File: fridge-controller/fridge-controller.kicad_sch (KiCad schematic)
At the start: 9 parts, among them U1 AMS1117-5.0, U2 Arduino_Pro_Mini, U3 SFH6156-2

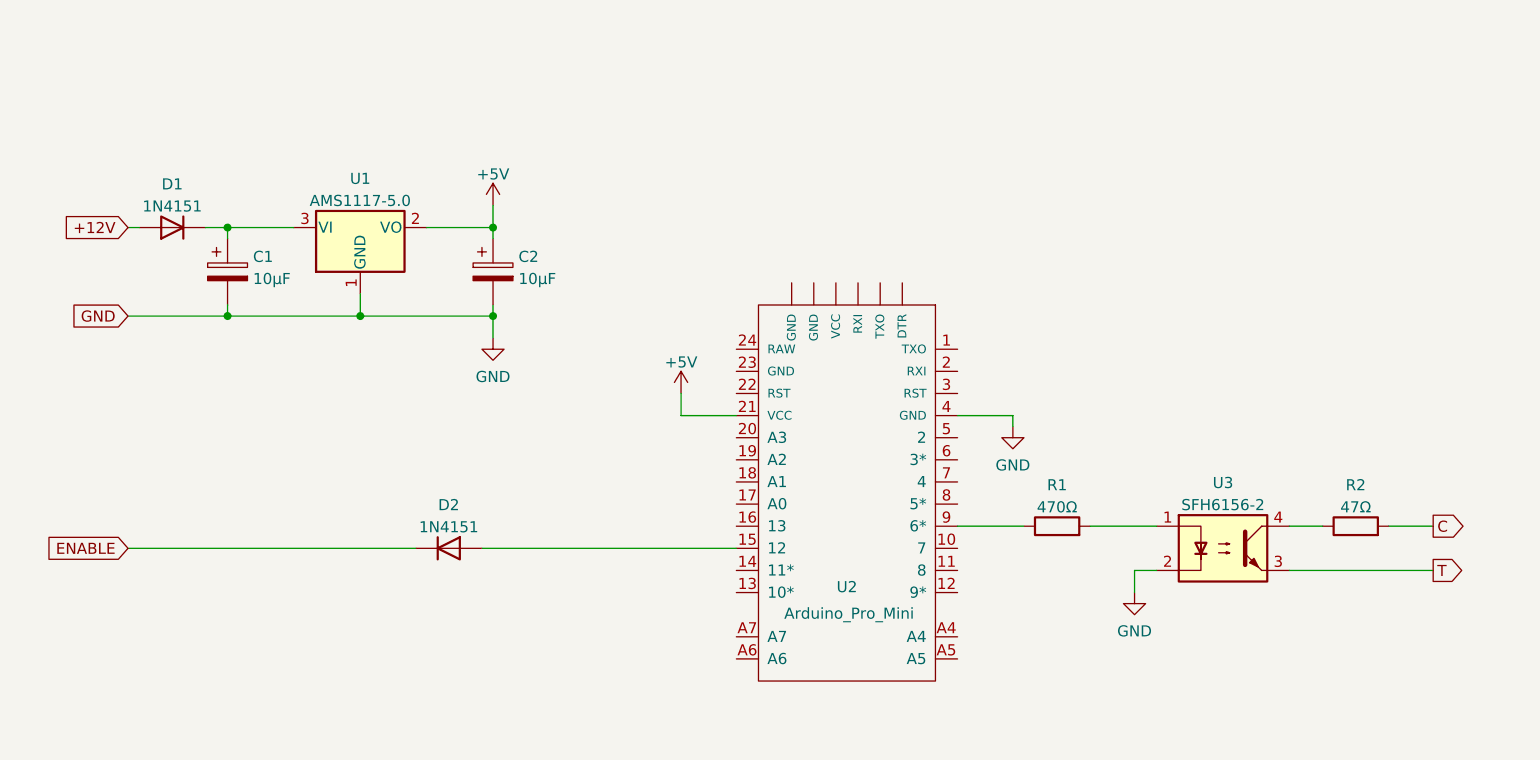
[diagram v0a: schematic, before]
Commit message: Updated fridge-controller
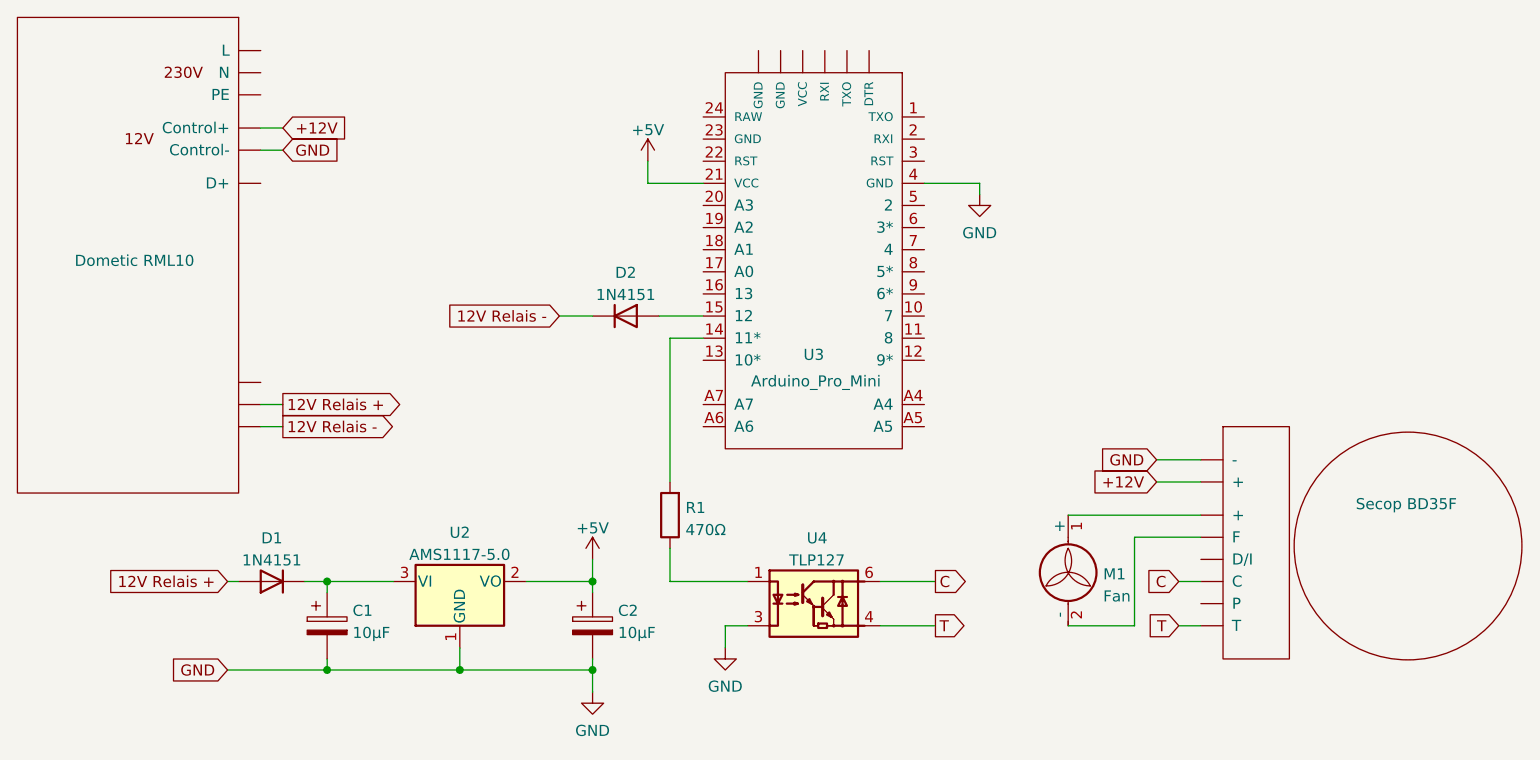
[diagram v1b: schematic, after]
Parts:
- removed R2: 47Ω, symbol Device:R
- removed U3: SFH6156-2, Package_DIP:DIP-4_W7.62mm, symbol Isolator:SFH617A-2
- added M1: Fan, symbol Motor:Fan
- added U1: Dometic RML10, symbol microfarad-de:Dometic_Fridge_2
- added U4: TLP127, Package_SO:MFSOP6-4_4.4x3.6mm_P1.27mm, symbol Isolator:TLP127
- added U5: Secop BD35F, symbol microfarad-de:Isotherm
- renumbered U1 to U2, U2 to U3
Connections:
- net +12V: now also U1. (PE), U5. (T); no longer D1.2 (A)
- net C: now also U4.6, U5. (T)
- net GND: now also U1. (PE), U4.3, U5. (T)
- net T: now also U4.4, U5. (T)
- net at R1.1: now also U4.1; no longer U3.9 (6*)
- net at R1.2: now also U3.14 (11*)
- net ENABLE renamed 12V Relais -
- net 12V Relais -: now also U1. (PE)
- new net: M1.1 (+), U5. (T)
- new net: M1.2 (-), U5. (T)
- new net 12V Relais +: D1.2 (A), U1. (PE)
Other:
- moved on the sheet: C1, C2, D1, D2, R1, U2, U3

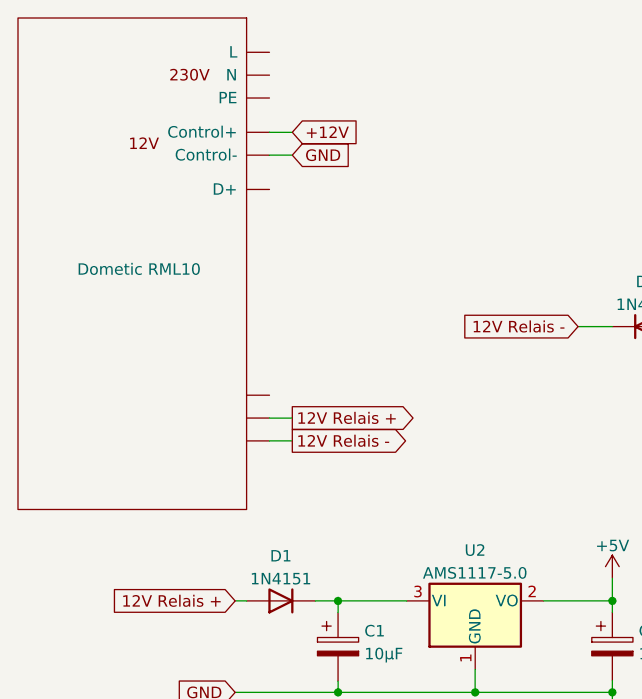
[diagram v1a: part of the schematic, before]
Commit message: Added Dometic RML10 to symbol library
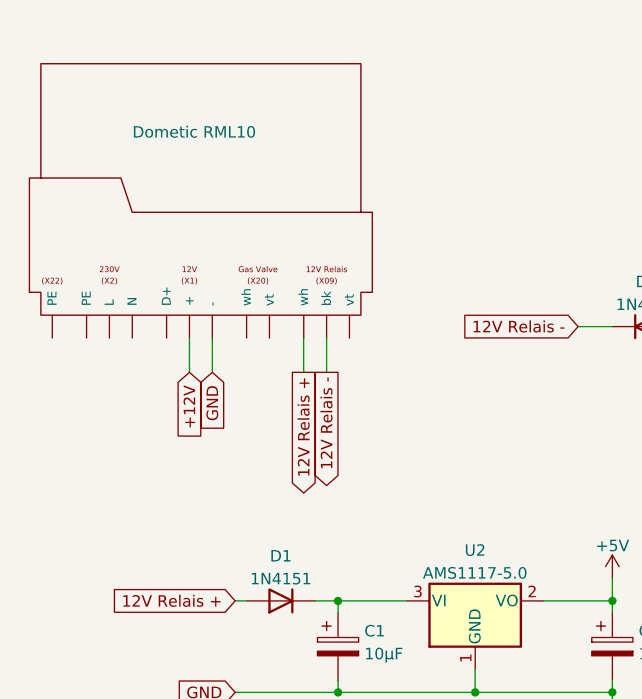
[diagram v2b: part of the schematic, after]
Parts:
- removed U1: Dometic RML10, symbol microfarad-de:Dometic_Fridge_2
- added U?: Dometic RML10, symbol microfarad-de:Dometic RML10
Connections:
- net +12V: now also U?. (wh)
- net 12V Relais +: now also U?. (wh)
- net 12V Relais -: now also U?. (wh)
- net GND: now also U?. (wh)
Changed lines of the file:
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@@
   (title_block
     (title "Secop BD35F Compressor Speed Controller")
-    (date "2025-02-09")
+    (date "2025-02-10")
     (company "Copyright (C) 2025, Karim Hraibi")
     (comment 1 "Enables variable speed control over 5 kHz PWM signal.")
@@
     (stroke (width 0) (type default) (color 0 0 0 0))
   )
-  (wire (pts (xy 46.99 27.94) (xy 49.53 27.94))
-    (stroke (width 0) (type default) (color 0 0 0 0))
-  )
   (wire (pts (xy 118.11 85.09) (xy 124.46 85.09))
     (stroke (width 0) (type default) (color 0 0 0 0))
@@
     (stroke (width 0) (type default) (color 0 0 0 0))
   )
-  (wire (pts (xy 46.99 30.48) (xy 49.53 30.48))
+  (wire (pts (xy 38.1 50.8) (xy 38.1 54.61))
     (stroke (width 0) (type default) (color 0 0 0 0))
   )
@@
     (stroke (width 0) (type default) (color 0 0 0 0))
   )
-  (wire (pts (xy 46.99 62.23) (xy 49.53 62.23))
-    (stroke (width 0) (type default) (color 0 0 0 0))
-  )
   (wire (pts (xy 139.7 72.39) (xy 154.94 72.39))
     (stroke (width 0) (type default) (color 0 0 0 0))
@@
     (stroke (width 0) (type default) (color 0 0 0 0))
   )
+  (wire (pts (xy 40.64 50.8) (xy 40.64 54.61))
+    (stroke (width 0) (type default) (color 0 0 0 0))
+  )
   (wire (pts (xy 69.85 87.63) (xy 69.85 90.17))
     (stroke (width 0) (type default) (color 0 0 0 0))
@@
     (stroke (width 0) (type default) (color 0 0 0 0))
   )
+  (wire (pts (xy 50.8 50.8) (xy 50.8 54.61))
+    (stroke (width 0) (type default) (color 0 0 0 0))
+  )
   (wire (pts (xy 85.09 77.47) (xy 85.09 80.01))
     (stroke (width 0) (type default) (color 0 0 0 0))
@@
     (stroke (width 0) (type default) (color 0 0 0 0))
   )
-  (wire (pts (xy 46.99 59.69) (xy 49.53 59.69))
-    (stroke (width 0) (type default) (color 0 0 0 0))
-  )
   (wire (pts (xy 54.61 90.17) (xy 69.85 90.17))
     (stroke (width 0) (type default) (color 0 0 0 0))
@@
     (stroke (width 0) (type default) (color 0 0 0 0))
   )
-  (global_label "+12V" (shape input) (at 49.53 27.94 0) (fields_autoplaced)
-    (effects (font (size 1.27 1.27)) (justify left))
-    (property "Intersheet References" "${INTERSHEET_REFS}" (id 0) (at 57.0231 28.0194 0)
-      (effects (font (size 1.27 1.27)) (justify left) hide)
+  (wire (pts (xy 53.34 50.8) (xy 53.34 54.61))
+    (stroke (width 0) (type default) (color 0 0 0 0))
+  )
+  (global_label "+12V" (shape input) (at 38.1 54.61 270) (fields_autoplaced)
+    (effects (font (size 1.27 1.27)) (justify right))
+    (property "Intersheet References" "${INTERSHEET_REFS}" (id 0) (at 38.0206 62.1031 90)
+      (effects (font (size 1.27 1.27)) (justify right) hide)
     )
   )
@@
     )
   )
-  (global_label "12V Relais -" (shape output) (at 49.53 62.23 0) (fields_autoplaced)
-    (effects (font (size 1.27 1.27)) (justify left))
-    (property "Intersheet References" "${INTERSHEET_REFS}" (id 0) (at 64.7641 62.1506 0)
-      (effects (font (size 1.27 1.27)) (justify left) hide)
+  (global_label "12V Relais -" (shape output) (at 53.34 54.61 270) (fields_autoplaced)
+    (effects (font (size 1.27 1.27)) (justify right))
+    (property "Intersheet References" "${INTERSHEET_REFS}" (id 0) (at 53.4194 69.8441 90)
+      (effects (font (size 1.27 1.27)) (justify right) hide)
     )
   )
@@
     )
   )
-  (global_label "12V Relais +" (shape output) (at 49.53 59.69 0) (fields_autoplaced)
-    (effects (font (size 1.27 1.27)) (justify left))
-    (property "Intersheet References" "${INTERSHEET_REFS}" (id 0) (at 64.7641 59.6106 0)
-      (effects (font (size 1.27 1.27)) (justify left) hide)
+  (global_label "12V Relais +" (shape output) (at 50.8 54.61 270) (fields_autoplaced)
+    (effects (font (size 1.27 1.27)) (justify right))
+    (property "Intersheet References" "${INTERSHEET_REFS}" (id 0) (at 50.8794 69.8441 90)
+      (effects (font (size 1.27 1.27)) (justify right) hide)
     )
   )
@@
     )
   )
-  (global_label "GND" (shape input) (at 49.53 30.48 0) (fields_autoplaced)
-    (effects (font (size 1.27 1.27)) (justify left))
-    (property "Intersheet References" "${INTERSHEET_REFS}" (id 0) (at 55.8136 30.5594 0)
-      (effects (font (size 1.27 1.27)) (justify left) hide)
+  (global_label "GND" (shape input) (at 40.64 54.61 270) (fields_autoplaced)
+    (effects (font (size 1.27 1.27)) (justify right))
+    (property "Intersheet References" "${INTERSHEET_REFS}" (id 0) (at 40.5606 60.8936 90)
+      (effects (font (size 1.27 1.27)) (justify right) hide)
     )
   )
@@
     (pin "1")
     (pin "2")
-  )
-  (symbol (lib_id "microfarad-de:Dometic_Fridge_2") (at 31.75 41.91 0) (mirror y) (unit 1)
-    (in_bom yes) (on_board yes)
-    (property "Reference" "U1" (id 0) (at 31.75 33.02 0)
-      (effects (font (size 1.27 1.27)) hide)
-    )
-    (property "Value" "Dometic RML10" (id 1) (at 39.37 43.18 0)
-      (effects (font (size 1.27 1.27)) (justify left))
-    )
-    (property "Footprint" "" (id 2) (at 17.78 33.02 0)
-      (effects (font (size 1.27 1.27)) hide)
-    )
-    (property "Datasheet" "" (id 3) (at 17.78 33.02 0)
-      (effects (font (size 1.27 1.27)) hide)
-    )
-    (pin "")
-    (pin "")
-    (pin "")
-    (pin "")
-    (pin "")
-    (pin "")
-    (pin "")
-    (pin "")
-    (pin "")
   )
   (symbol (lib_id "Isolator:TLP127") (at 110.49 82.55 0) (unit 1)
@@
     (pin "1")
   )
+  (symbol (lib_id "microfarad-de:Dometic RML10") (at 36.83 36.83 0) (unit 1)
+    (in_bom yes) (on_board yes)
+    (property "Reference" "U?" (id 0) (at 36.83 27.94 0)
+      (effects (font (size 1.27 1.27)) hide)
+    )
+    (property "Value" "Dometic RML10" (id 1) (at 31.75 27.94 0)
+      (effects (font (size 1.27 1.27)) (justify left))
+    )
+    (property "Footprint" "" (id 2) (at 50.8 27.94 0)
+      (effects (font (size 1.27 1.27)) hide)
+    )
+    (property "Datasheet" "" (id 3) (at 50.8 27.94 0)
+      (effects (font (size 1.27 1.27)) hide)
+    )
+    (pin "")
+    (pin "")
+    (pin "")
+    (pin "")
+    (pin "")
+    (pin "")
+    (pin "")
+    (pin "")
+    (pin "")
+    (pin "")
+    (pin "")
+    (pin "")
+  )
   (sheet_instances
     (path "/" (page "1"))
@@
       (reference "R1") (unit 1) (value "470Ω") (footprint "")
     )
-    (path "/75f77b61-ec76-4952-a72e-f5df01a44554"
-      (reference "U1") (unit 1) (value "Dometic RML10") (footprint "")
-    )
     (path "/b8b41635-00c1-442e-ba06-4137bff20311"
       (reference "U2") (unit 1) (value "AMS1117-5.0") (footprint "Package_TO_SOT_SMD:SOT-223-3_TabPin2")
@@
       (reference "U5") (unit 1) (value "Secop BD35F") (footprint "")
     )
-  )
+    (path "/f34b6659-deac-4243-935d-e65feaddf571"
+      (reference "U?") (unit 1) (value "Dometic RML10") (footprint "")
+    )
+  )

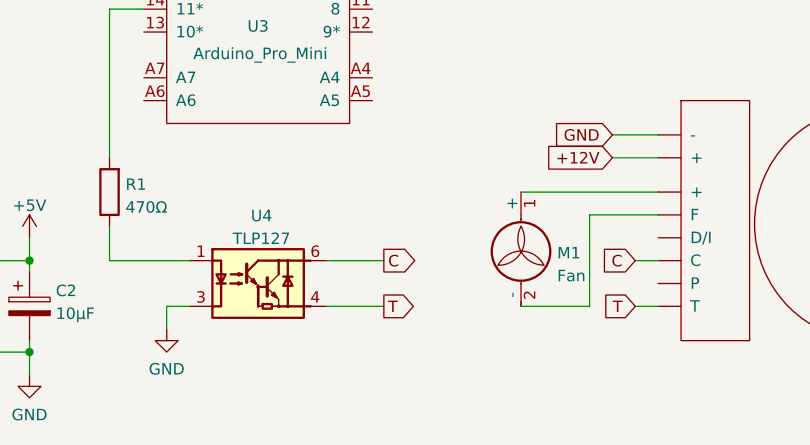
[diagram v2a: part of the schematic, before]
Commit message: Updated fridge-controller
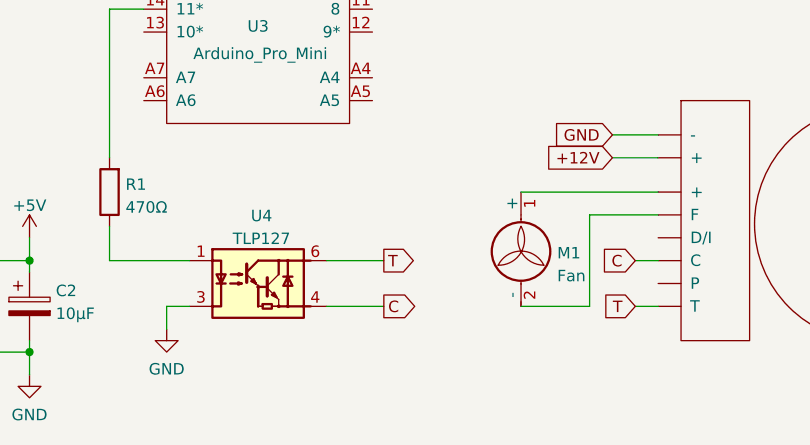
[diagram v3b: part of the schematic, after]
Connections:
- net C: now also U4.4; no longer U4.6
- net T: now also U4.6; no longer U4.4
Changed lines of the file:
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@@
   (title_block
     (title "Secop BD35F Compressor Speed Controller")
-    (date "2025-02-10")
+    (date "2025-02-14")
     (company "Copyright (C) 2025, Karim Hraibi")
     (comment 1 "Enables variable speed control over 5 kHz PWM signal.")
@@
     )
   )
-  (global_label "C" (shape output) (at 124.46 80.01 0) (fields_autoplaced)
+  (global_label "T" (shape output) (at 124.46 80.01 0) (fields_autoplaced)
     (effects (font (size 1.27 1.27)) (justify left))
-    (property "Intersheet References" "${INTERSHEET_REFS}" (id 0) (at 128.1431 79.9306 0)
+    (property "Intersheet References" "${INTERSHEET_REFS}" (id 0) (at 127.8407 79.9306 0)
       (effects (font (size 1.27 1.27)) (justify left) hide)
     )
@@
     )
   )
-  (global_label "T" (shape output) (at 124.46 85.09 0) (fields_autoplaced)
+  (global_label "C" (shape output) (at 124.46 85.09 0) (fields_autoplaced)
     (effects (font (size 1.27 1.27)) (justify left))
-    (property "Intersheet References" "${INTERSHEET_REFS}" (id 0) (at 127.8407 85.0106 0)
+    (property "Intersheet References" "${INTERSHEET_REFS}" (id 0) (at 128.1431 85.0106 0)
       (effects (font (size 1.27 1.27)) (justify left) hide)
     )
